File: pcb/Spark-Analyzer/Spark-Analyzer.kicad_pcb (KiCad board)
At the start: 4 copper layers, 46.5 x 40 mm, 82 parts, among them IC2 FUSB302MPX, IC3 CC6904SO-10A, IC4 TPS62175DQCT, IC5 ESP32-C3FH4, J1 GT-USB-7010, J2 TC2050-IDC, J3 KF350-3.5-2P, J5 Conn_01x06, Q1 DTC143ECA-TP, Q2 DMP3017SFG-7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

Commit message: First app release and updated PCBA
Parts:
- removed ?: Product Stamp, personal:Product Stamp
- removed AE1: ANT3216LL00R2400A, Resistor_SMD:R_1206_3216Metric_Pad1.30x1.75mm_HandSolder
- removed R10: 0, Resistor_SMD:R_0805_2012Metric_Pad1.20x1.40mm_HandSolder
- removed R15: DNF_0402, Resistor_SMD:R_0402_1005Metric
- removed TP6, TP7, TP9: TestPoint, TestPoint:TestPoint_Pad_D1.0mm
- added D4: Green_0603, LED_SMD:LED_0603_1608Metric, F.Cu at (202.6, 119.0)
- added G***: LOGO, personal:reset, F.Cu at (184.0, 134.0)
- added G***: LOGO, personal:USBC, F.Cu at (204.0, 103.5)
- added R22: 2.7k, Resistor_SMD:R_0402_1005Metric, F.Cu at (202.2, 117.5)
- added REF**: Product Stamp, personal:Product Stamp, B.Cu at (222.5, 125.5)
- D3: value Green_0603 -> Yellow_0603
- moved S2 2.20 mm to (187.1, 123.4)
- moved D3 1.37 mm to (212.4, 119.4), turned to 90 degrees
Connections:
- C10 pad 1: Net-(C10-Pad1) -> Net-(AE2-A)
- L2 pad 1: Net-(C10-Pad1) -> Net-(AE2-A)
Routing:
- net Net-(C10-Pad1): track 5.26 -> 0.00 mm
- net /Microcontroller/EN: track 57.3 -> 52.6 mm
- net Net-(AE2-A): track 1.15 -> 5.74 mm
- net Net-(Q2-D_1): track 11.3 -> 7.51 mm, vias 2 -> 0
- net /Current Sensor + Output Control/VOUT: track 2.95 -> 0.00 mm
- net /Microcontroller/GPIO9: track 36.0 -> 38.7 mm
- net /Microcontroller/GPIO3: track 34.1 -> 36.7 mm
- net Net-(AE1-PCB_Trace): track 2.12 -> 0.00 mm
- net Net-(D4-K): track 0.00 -> 1.51 mm
- net +3V3: track 101.7 -> 100.2 mm, vias 13 -> 11
- net GND: track 29.4 -> 28.6 mm, vias 26 -> 37
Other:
- board text added: "3V3"
- board text added: "8"
- board text added: "9"
- board text added: "GND"
- board text added: "RX"
- board text added: "SET"
- board text added: "TX"

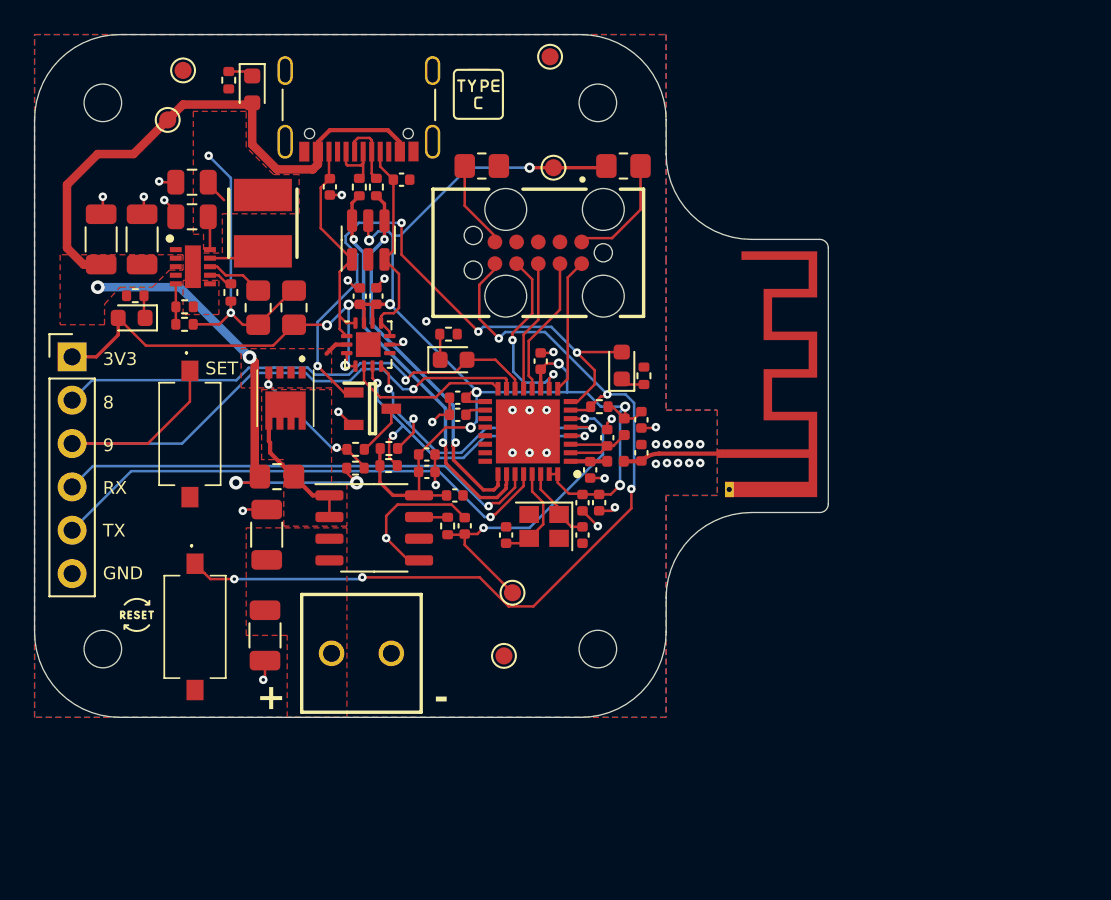
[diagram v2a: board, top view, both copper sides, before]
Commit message: Added silkscreen symbols and texts
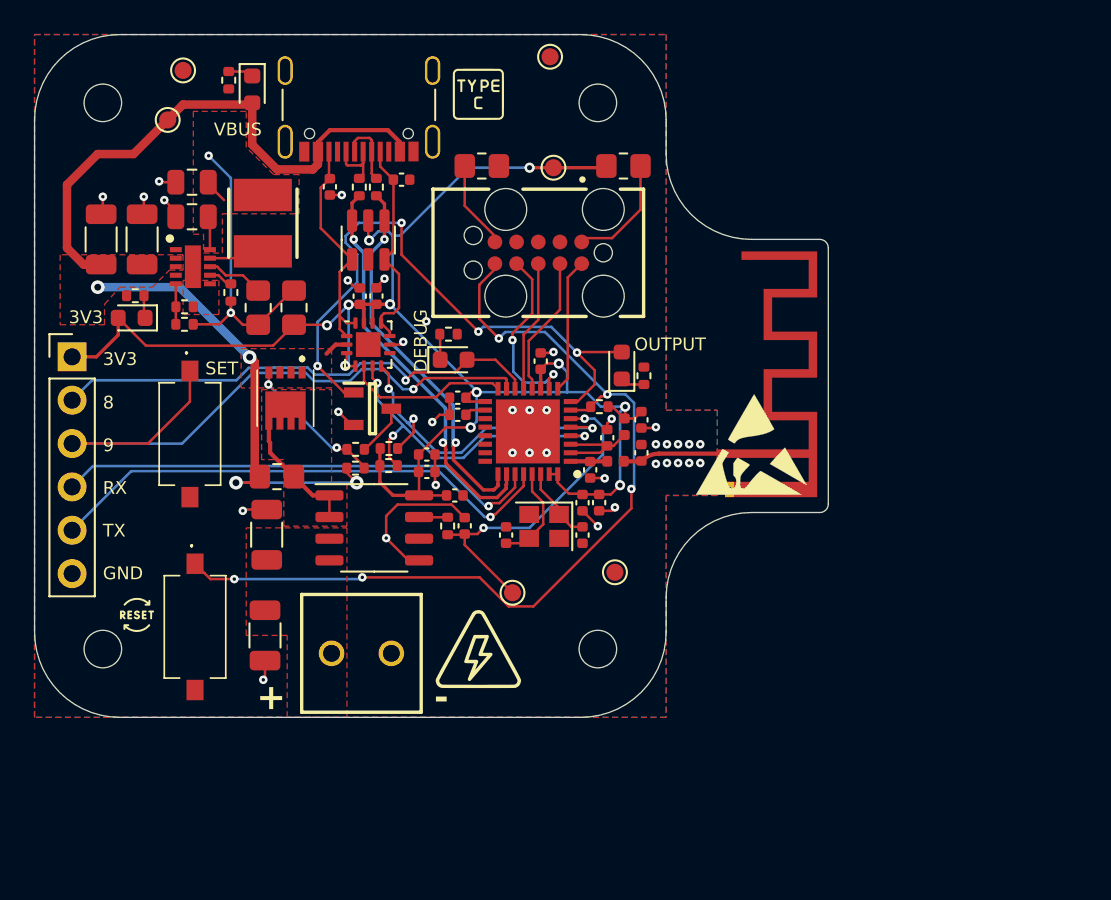
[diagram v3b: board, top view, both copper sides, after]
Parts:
- added  : LOGO, personal:highVoltage, F.Cu at (204.0, 136.0)
- added  : LOGO, personal:highVoltage, B.Cu at (204.0, 136.5)
- added G***: LOGO, personal:warning, B.Cu at (184.5, 138.0)
- added REF**: ESD-Logo_6.6x6mm_SilkScreen, Symbol:ESD-Logo_6.6x6mm_SilkScreen, F.Cu at (220.0, 124.0)
- moved TP10 8.14 mm to (212.0, 131.5)
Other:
- board text added: "DEBUG"
- board text added: "Do not place on conductive surfaces."
- board text added: "OUTPUT"
- board text added: "VBUS"

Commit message: Wired sensor and changed connector
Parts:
- removed C8: 100n, Capacitor_SMD:C_0402_1005Metric
- removed IC3: CC6904SO-10A, Package_SO:SOP-8_3.9x4.9mm_P1.27mm
- removed J3: KF350-3.5-2P, SamacSys_Parts:KF350352P
- removed R11, R9: 0, Resistor_SMD:R_0805_2012Metric_Pad1.20x1.40mm_HandSolder
- removed R8: 100, Resistor_SMD:R_0402_1005Metric
- removed REF**: ESD-Logo_6.6x6mm_SilkScreen, Symbol:ESD-Logo_6.6x6mm_SilkScreen
- removed REF**: Product Stamp, personal:Product Stamp
- removed TP8: TestPoint, TestPoint:TestPoint_Pad_D1.0mm
- added IC1: INA260AIPWR, SamacSys_Parts:SOP65P640X120-16N, F.Cu at (235.4, 141.9)
- added R10: 10k, Resistor_SMD:R_0402_1005Metric, F.Cu at (232.4, 146.3)
- added R15: 10k, Resistor_SMD:R_0402_1005Metric, F.Cu at (232.4, 148.3)
- J2: value TC2050-IDC -> 2060-452_998-404; footprint SamacSys_Parts:TC2050-IDC -> SamacSys_Parts:2060452998404
- moved J2 20.9 mm to (197.5, 133.1), turned to 90 degrees
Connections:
- IC5 pad 10: Net-(IC5-MTDI) -> unconnected-(IC5-MTDI-Pad10)
- IC5 pad 12: Net-(IC5-MTCK) -> unconnected-(IC5-MTCK-Pad12)
- IC5 pad 13: Net-(IC5-MTDO) -> unconnected-(IC5-MTDO-Pad13)
- IC5 pad 6: /Current Sensor + Output Control/V_CURRENT -> /Microcontroller/V_CURRENT
- IC5 pad 9: Net-(IC5-MTMS) -> unconnected-(IC5-MTMS-Pad9)
- J2 pad 1: Net-(J2-VTref) -> /Current Sensor + Output Control/VOUT
- J2 pad 2: Net-(IC5-MTMS) -> unconnected-(J2-1.2-Pad2)
- J2 pad 4: Net-(IC5-MTCK) -> unconnected-(J2-2.2-Pad4)
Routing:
- net /Microcontroller/V_CURRENT: track 0.00 -> 19.3 mm, vias 0 -> 2
- net /Current Sensor + Output Control/V_CURRENT: track 19.3 -> 0.00 mm, vias 2 -> 0
- net (no net): track 0.00 -> 13.0 mm
- net unconnected-(IC5-MTDI-Pad10): track 0.00 -> 11.0 mm, vias 0 -> 2
- net Net-(IC5-MTDI): track 11.0 -> 0.00 mm, vias 2 -> 0
- net unconnected-(IC5-MTCK-Pad12): track 0.00 -> 8.17 mm
- net Net-(IC5-MTCK): track 8.17 -> 0.00 mm
- net unconnected-(IC5-MTMS-Pad9): track 0.00 -> 7.91 mm
- net Net-(IC5-MTMS): track 7.91 -> 0.00 mm
- net unconnected-(IC5-MTDO-Pad13): track 0.00 -> 7.69 mm
- net Net-(IC5-MTDO): track 7.69 -> 0.00 mm
- net Net-(J2-VTref): track 6.48 -> 0.00 mm
- net Net-(J2-GNDDetect): track 4.84 -> 0.00 mm
- net Net-(IC3-OUT): track 1.66 -> 0.00 mm
